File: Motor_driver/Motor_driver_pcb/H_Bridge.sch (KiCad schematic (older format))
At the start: 8 parts, among them Q1 IRF9540N, Q2 IRF540N, Q3 IRF9540N, Q4 IRF540N

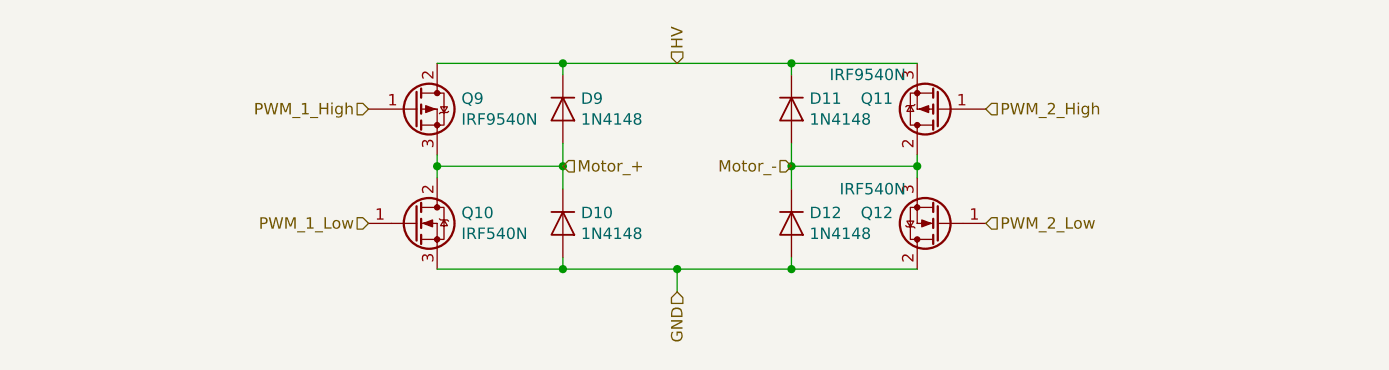
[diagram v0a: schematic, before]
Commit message: update driver schema add  uc config
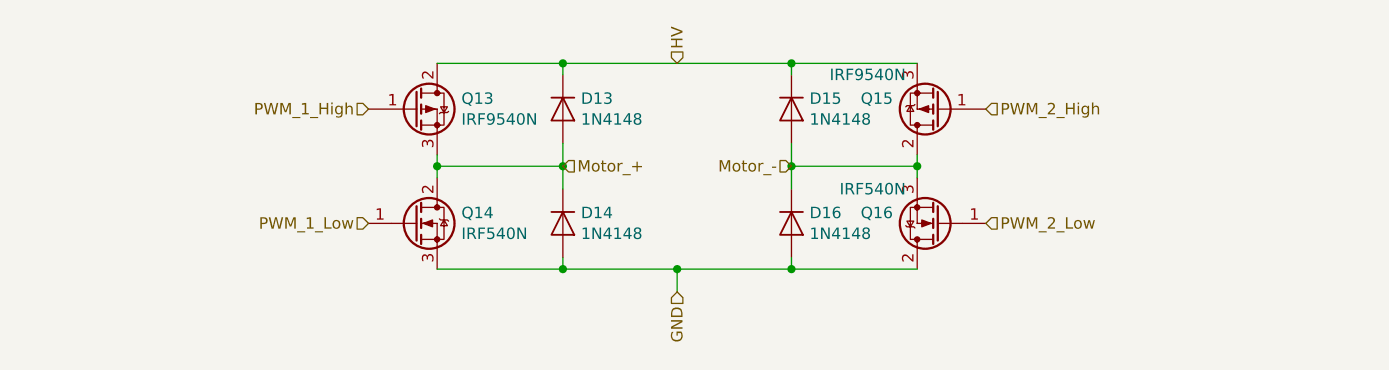
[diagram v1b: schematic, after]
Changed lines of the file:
@@
 $Descr A4 11693 8268
 encoding utf-8
-Sheet 4 5
+Sheet 5 5
 Title ""
 Date ""
@@
 AR Path="/5C9F4B73/5C9E42AA" Ref="Q10"  Part="1"
 AR Path="/5C9F4B7D/5C9E42AA" Ref="Q14"  Part="1"
-F 0 "Q10" H 4056 3046 50  0000 L CNN
+F 0 "Q14" H 4056 3046 50  0000 L CNN
 F 1 "IRF540N" H 4056 2955 50  0000 L CNN
 F 2 "Package_TO_SOT_THT:TO-220-3_Vertical" H 4100 2925 50  0001 L CIN
@@
 AR Path="/5C9F4B73/5C9E4811" Ref="Q9"  Part="1"
 AR Path="/5C9F4B7D/5C9E4811" Ref="Q13"  Part="1"
-F 0 "Q9" H 4056 2546 50  0000 L CNN
+F 0 "Q13" H 4056 2546 50  0000 L CNN
 F 1 "IRF9540N" H 4056 2455 50  0000 L CNN
 F 2 "Package_TO_SOT_THT:TO-220-3_Vertical" H 4050 2425 50  0001 L CIN
@@
 AR Path="/5C9F4B73/5C9E549E" Ref="D9"  Part="1"
 AR Path="/5C9F4B7D/5C9E549E" Ref="D13"  Part="1"
-F 0 "D9" V 4454 2579 50  0000 L CNN
+F 0 "D13" V 4454 2579 50  0000 L CNN
 F 1 "1N4148" V 4545 2579 50  0000 L CNN
 F 2 "Diode_THT:D_DO-35_SOD27_P7.62mm_Horizontal" H 4500 2325 50  0001 C CNN
@@
 AR Path="/5C9F4B73/5C9E5F82" Ref="D10"  Part="1"
 AR Path="/5C9F4B7D/5C9E5F82" Ref="D14"  Part="1"
-F 0 "D10" V 4454 3079 50  0000 L CNN
+F 0 "D14" V 4454 3079 50  0000 L CNN
 F 1 "1N4148" V 4545 3079 50  0000 L CNN
 F 2 "Diode_THT:D_DO-35_SOD27_P7.62mm_Horizontal" H 4500 2825 50  0001 C CNN
@@
 AR Path="/5C9F4B73/5C9E6D79" Ref="Q11"  Part="1"
 AR Path="/5C9F4B7D/5C9E6D79" Ref="Q15"  Part="1"
-F 0 "Q11" H 6356 2454 50  0000 L CNN
+F 0 "Q15" H 6356 2454 50  0000 L CNN
 F 1 "IRF9540N" H 6300 2350 50  0000 L CNN
 F 2 "Package_TO_SOT_THT:TO-220-3_Vertical" H 6350 2425 50  0001 L CIN
@@
 AR Path="/5C9F4B73/5C9E8C92" Ref="Q12"  Part="1"
 AR Path="/5C9F4B7D/5C9E8C92" Ref="Q16"  Part="1"
-F 0 "Q12" H 6356 2954 50  0000 L CNN
+F 0 "Q16" H 6356 2954 50  0000 L CNN
 F 1 "IRF540N" H 6300 2850 50  0000 L CNN
 F 2 "Package_TO_SOT_THT:TO-220-3_Vertical" H 6400 2925 50  0001 L CIN
@@
 AR Path="/5C9F4B73/5C9EAA23" Ref="D11"  Part="1"
 AR Path="/5C9F4B7D/5C9EAA23" Ref="D15"  Part="1"
-F 0 "D11" V 5454 2579 50  0000 L CNN
+F 0 "D15" V 5454 2579 50  0000 L CNN
 F 1 "1N4148" V 5545 2579 50  0000 L CNN
 F 2 "Diode_THT:D_DO-35_SOD27_P7.62mm_Horizontal" H 5500 2325 50  0001 C CNN
@@
 AR Path="/5C9F4B73/5C9EC3FB" Ref="D12"  Part="1"
 AR Path="/5C9F4B7D/5C9EC3FB" Ref="D16"  Part="1"
-F 0 "D12" V 5454 3079 50  0000 L CNN
+F 0 "D16" V 5454 3079 50  0000 L CNN
 F 1 "1N4148" V 5545 3079 50  0000 L CNN
 F 2 "Diode_THT:D_DO-35_SOD27_P7.62mm_Horizontal" H 5500 2825 50  0001 C CNN

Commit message: update schema, create PCB
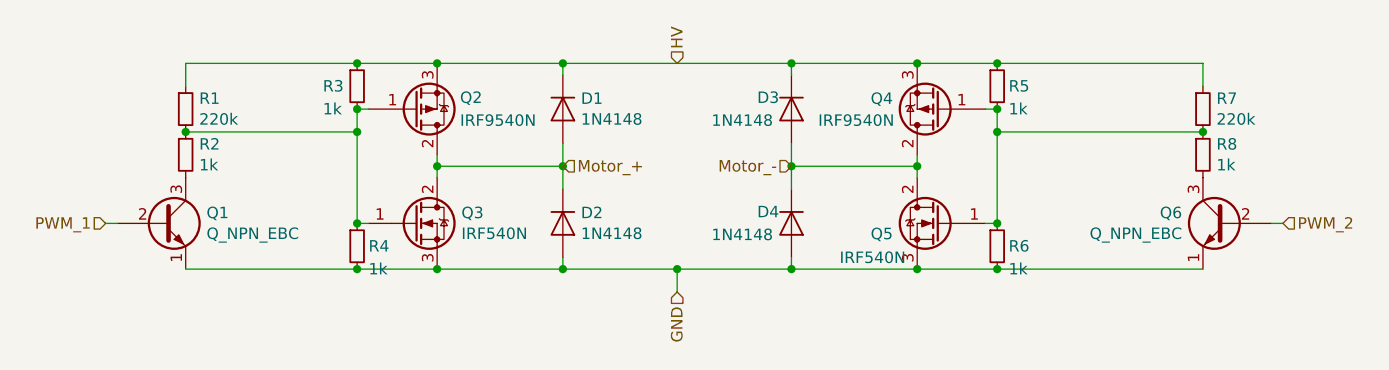
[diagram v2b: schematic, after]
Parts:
- added Q1, Q6: Q_NPN_EBC, Package_TO_SOT_THT:TO-92, symbol Device:Q_NPN_EBC
- added R1, R7: 220k, Resistor_SMD:R_0805_2012Metric_Pad1.15x1.40mm_HandSolder, symbol Device:R_Small
- added R2, R3, R4, R5, R6, R8: 1k, Resistor_SMD:R_0805_2012Metric_Pad1.15x1.40mm_HandSolder, symbol Device:R_Small
- renumbered Q1 to Q2, Q2 to Q3, Q3 to Q4, Q4 to Q5
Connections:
- net PWM_1_Low is gone; now on an unnamed net: Q3.1 (G)
- net PWM_2_Low is gone; now on an unnamed net: Q5.1 (G)
- net GND: now also Q5.3 (S), Q1.1 (E), Q6.1 (E), R4.2, R6.2; no longer Q5.2 (D)
- net HV: now also Q2.3 (S), R1.1, R3.1, R5.1, R7.1; no longer Q2.2 (D)
- net Motor_+: now also Q2.2 (D); no longer Q2.3 (S)
- net Motor_-: now also Q5.2 (D); no longer Q5.3 (S)
- net PWM_1_High: no longer names the net of Q2.1 (G)
- net PWM_1_High: now also R1.2, R2.1, R3.2, R4.1
- net PWM_2_High: no longer names the net of Q4.1 (G)
- net PWM_2_High: now also R5.2, R6.1, R7.2, R8.1
- new net: Q1.3 (C), R2.2
- new net: Q6.3 (C), R8.2
- new net PWM_1: Q1.2 (B)
- new net PWM_2: Q6.2 (B)

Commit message: finish schema and PCB update uC configuration
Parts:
- Q1, Q6: value Q_NPN_EBC -> 2N2222
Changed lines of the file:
@@
 AR Path="/5CA227B5/5CC73221" Ref="Q19"  Part="1"
 F 0 "Q1" H 2941 3046 50  0000 L CNN
-F 1 "Q_NPN_EBC" H 2941 2955 50  0000 L CNN
+F 1 "2N2222" H 2941 2955 50  0000 L CNN
 F 2 "Package_TO_SOT_THT:TO-92" H 2950 3100 50  0001 C CNN
 F 3 "~" H 2750 3000 50  0001 C CNN
@@
 AR Path="/5CA227B5/5CC746B3" Ref="Q24"  Part="1"
 F 0 "Q6" H 7591 3046 50  0000 L CNN
-F 1 "Q_NPN_EBC" H 7591 2955 50  0000 L CNN
+F 1 "2N2222" H 7591 2955 50  0000 L CNN
 F 2 "Package_TO_SOT_THT:TO-92" H 7600 3100 50  0001 C CNN
 F 3 "~" H 7400 3000 50  0001 C CNN

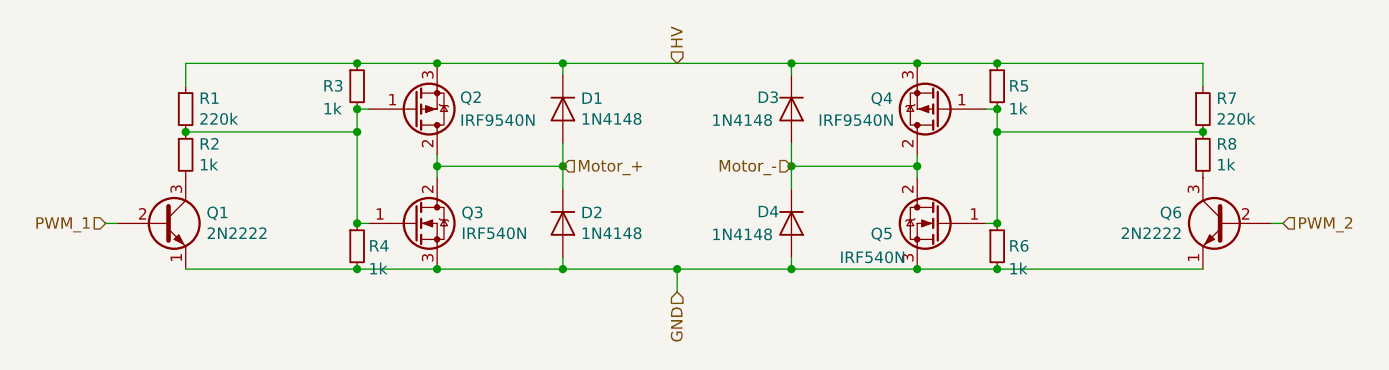
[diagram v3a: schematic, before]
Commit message: add BT_module PCB add Gerbera files
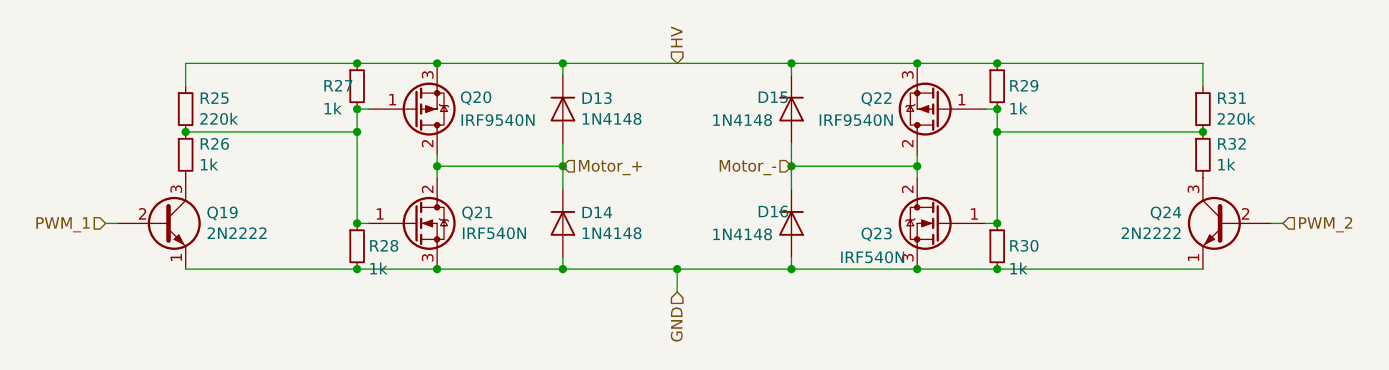
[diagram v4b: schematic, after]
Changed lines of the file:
@@
 AR Path="/5CA1B151/5C9E42AA" Ref="Q15"  Part="1"
 AR Path="/5CA227B5/5C9E42AA" Ref="Q21"  Part="1"
-F 0 "Q3" H 4056 3046 50  0000 L CNN
+F 0 "Q21" H 4056 3046 50  0000 L CNN
 F 1 "IRF540N" H 4056 2955 50  0000 L CNN
 F 2 "Package_TO_SOT_THT:TO-220-3_Vertical" H 4100 2925 50  0001 L CIN
@@
 AR Path="/5CA1B151/5C9E4811" Ref="Q14"  Part="1"
 AR Path="/5CA227B5/5C9E4811" Ref="Q20"  Part="1"
-F 0 "Q2" H 4050 2450 50  0000 L CNN
+F 0 "Q20" H 4050 2450 50  0000 L CNN
 F 1 "IRF9540N" H 4050 2550 50  0000 L CNN
 F 2 "Package_TO_SOT_THT:TO-220-3_Vertical" H 4050 2425 50  0001 L CIN
@@
 AR Path="/5CA1B151/5C9E549E" Ref="D9"  Part="1"
 AR Path="/5CA227B5/5C9E549E" Ref="D13"  Part="1"
-F 0 "D1" V 4454 2579 50  0000 L CNN
+F 0 "D13" V 4454 2579 50  0000 L CNN
 F 1 "1N4148" V 4545 2579 50  0000 L CNN
 F 2 "Diode_THT:D_DO-35_SOD27_P7.62mm_Horizontal" H 4500 2325 50  0001 C CNN
@@
 AR Path="/5CA1B151/5C9E5F82" Ref="D10"  Part="1"
 AR Path="/5CA227B5/5C9E5F82" Ref="D14"  Part="1"
-F 0 "D2" V 4454 3079 50  0000 L CNN
+F 0 "D14" V 4454 3079 50  0000 L CNN
 F 1 "1N4148" V 4545 3079 50  0000 L CNN
 F 2 "Diode_THT:D_DO-35_SOD27_P7.62mm_Horizontal" H 4500 2825 50  0001 C CNN
@@
 AR Path="/5CA1B151/5C9E6D79" Ref="Q16"  Part="1"
 AR Path="/5CA227B5/5C9E6D79" Ref="Q22"  Part="1"
-F 0 "Q4" H 6356 2454 50  0000 L CNN
+F 0 "Q22" H 6356 2454 50  0000 L CNN
 F 1 "IRF9540N" H 6350 2550 50  0000 L CNN
 F 2 "Package_TO_SOT_THT:TO-220-3_Vertical" H 6350 2425 50  0001 L CIN
@@
 AR Path="/5CA1B151/5C9E8C92" Ref="Q17"  Part="1"
 AR Path="/5CA227B5/5C9E8C92" Ref="Q23"  Part="1"
-F 0 "Q5" H 6356 2954 50  0000 L CNN
+F 0 "Q23" H 6356 2954 50  0000 L CNN
 F 1 "IRF540N" H 6300 2850 50  0000 L CNN
 F 2 "Package_TO_SOT_THT:TO-220-3_Vertical" H 6400 2925 50  0001 L CIN
@@
 AR Path="/5CA1B151/5C9EAA23" Ref="D11"  Part="1"
 AR Path="/5CA227B5/5C9EAA23" Ref="D15"  Part="1"
-F 0 "D3" V 5450 2350 50  0000 L CNN
+F 0 "D15" V 5450 2350 50  0000 L CNN
 F 1 "1N4148" V 5550 2150 50  0000 L CNN
 F 2 "Diode_THT:D_DO-35_SOD27_P7.62mm_Horizontal" H 5500 2325 50  0001 C CNN
@@
 AR Path="/5CA1B151/5C9EC3FB" Ref="D12"  Part="1"
 AR Path="/5CA227B5/5C9EC3FB" Ref="D16"  Part="1"
-F 0 "D4" V 5450 2850 50  0000 L CNN
+F 0 "D16" V 5450 2850 50  0000 L CNN
 F 1 "1N4148" V 5550 2650 50  0000 L CNN
 F 2 "Diode_THT:D_DO-35_SOD27_P7.62mm_Horizontal" H 5500 2825 50  0001 C CNN
@@
 AR Path="/5CA1B151/5CA04B0F" Ref="R21"  Part="1"
 AR Path="/5CA227B5/5CA04B0F" Ref="R29"  Part="1"
-F 0 "R5" H 6450 2400 50  0000 L CNN
+F 0 "R29" H 6450 2400 50  0000 L CNN
 F 1 "1k" H 6450 2300 50  0000 L CNN
 F 2 "Resistor_SMD:R_0805_2012Metric_Pad1.15x1.40mm_HandSolder" H 6400 2400 50  0001 C CNN
@@
 AR Path="/5CA1B151/5CA04F40" Ref="R22"  Part="1"
 AR Path="/5CA227B5/5CA04F40" Ref="R30"  Part="1"
-F 0 "R6" H 6450 3100 50  0000 L CNN
+F 0 "R30" H 6450 3100 50  0000 L CNN
 F 1 "1k" H 6450 3000 50  0000 L CNN
 F 2 "Resistor_SMD:R_0805_2012Metric_Pad1.15x1.40mm_HandSolder" H 6400 3100 50  0001 C CNN
@@
 AR Path="/5CA1B151/5CA0523E" Ref="R20"  Part="1"
 AR Path="/5CA227B5/5CA0523E" Ref="R28"  Part="1"
-F 0 "R4" H 3650 3100 50  0000 L CNN
+F 0 "R28" H 3650 3100 50  0000 L CNN
 F 1 "1k" H 3650 3000 50  0000 L CNN
 F 2 "Resistor_SMD:R_0805_2012Metric_Pad1.15x1.40mm_HandSolder" H 3600 3100 50  0001 C CNN
@@
 AR Path="/5CA1B151/5CA057A9" Ref="R19"  Part="1"
 AR Path="/5CA227B5/5CA057A9" Ref="R27"  Part="1"
-F 0 "R3" H 3450 2400 50  0000 L CNN
+F 0 "R27" H 3450 2400 50  0000 L CNN
 F 1 "1k" H 3450 2300 50  0000 L CNN
 F 2 "Resistor_SMD:R_0805_2012Metric_Pad1.15x1.40mm_HandSolder" H 3600 2400 50  0001 C CNN
@@
 AR Path="/5CA1B151/5CABFFC4" Ref="R18"  Part="1"
 AR Path="/5CA227B5/5CABFFC4" Ref="R26"  Part="1"
-F 0 "R2" H 2909 2746 50  0000 L CNN
+F 0 "R26" H 2909 2746 50  0000 L CNN
 F 1 "1k" H 2909 2655 50  0000 L CNN
 F 2 "Resistor_SMD:R_0805_2012Metric_Pad1.15x1.40mm_HandSolder" H 2850 2700 50  0001 C CNN
@@
 AR Path="/5CA1B151/5CAC04F6" Ref="R17"  Part="1"
 AR Path="/5CA227B5/5CAC04F6" Ref="R25"  Part="1"
-F 0 "R1" H 2909 2546 50  0000 L CNN
+F 0 "R25" H 2909 2546 50  0000 L CNN
 F 1 "220k" H 2909 2455 50  0000 L CNN
 F 2 "Resistor_SMD:R_0805_2012Metric_Pad1.15x1.40mm_HandSolder" H 2850 2500 50  0001 C CNN
@@
 AR Path="/5CA1B151/5CBAE7DE" Ref="R24"  Part="1"
 AR Path="/5CA227B5/5CBAE7DE" Ref="R32"  Part="1"
-F 0 "R8" H 7359 2746 50  0000 L CNN
+F 0 "R32" H 7359 2746 50  0000 L CNN
 F 1 "1k" H 7359 2655 50  0000 L CNN
 F 2 "Resistor_SMD:R_0805_2012Metric_Pad1.15x1.40mm_HandSolder" H 7300 2700 50  0001 C CNN
@@
 AR Path="/5CA1B151/5CBAE7E4" Ref="R23"  Part="1"
 AR Path="/5CA227B5/5CBAE7E4" Ref="R31"  Part="1"
-F 0 "R7" H 7359 2546 50  0000 L CNN
+F 0 "R31" H 7359 2546 50  0000 L CNN
 F 1 "220k" H 7359 2455 50  0000 L CNN
 F 2 "Resistor_SMD:R_0805_2012Metric_Pad1.15x1.40mm_HandSolder" H 7300 2500 50  0001 C CNN
@@
 AR Path="/5CA1B151/5CC73221" Ref="Q13"  Part="1"
 AR Path="/5CA227B5/5CC73221" Ref="Q19"  Part="1"
-F 0 "Q1" H 2941 3046 50  0000 L CNN
+F 0 "Q19" H 2941 3046 50  0000 L CNN
 F 1 "2N2222" H 2941 2955 50  0000 L CNN
 F 2 "Package_TO_SOT_THT:TO-92" H 2950 3100 50  0001 C CNN
@@
 AR Path="/5CA1B151/5CC746B3" Ref="Q18"  Part="1"
 AR Path="/5CA227B5/5CC746B3" Ref="Q24"  Part="1"
-F 0 "Q6" H 7591 3046 50  0000 L CNN
+F 0 "Q24" H 7591 3046 50  0000 L CNN
 F 1 "2N2222" H 7591 2955 50  0000 L CNN
 F 2 "Package_TO_SOT_THT:TO-92" H 7600 3100 50  0001 C CNN

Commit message: add final parts and working code
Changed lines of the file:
@@
 AR Path="/5CA1B151/5C9E42AA" Ref="Q15"  Part="1"
 AR Path="/5CA227B5/5C9E42AA" Ref="Q21"  Part="1"
-F 0 "Q21" H 4056 3046 50  0000 L CNN
+F 0 "Q3" H 4056 3046 50  0000 L CNN
 F 1 "IRF540N" H 4056 2955 50  0000 L CNN
 F 2 "Package_TO_SOT_THT:TO-220-3_Vertical" H 4100 2925 50  0001 L CIN
@@
 AR Path="/5CA1B151/5C9E4811" Ref="Q14"  Part="1"
 AR Path="/5CA227B5/5C9E4811" Ref="Q20"  Part="1"
-F 0 "Q20" H 4050 2450 50  0000 L CNN
+F 0 "Q2" H 4050 2450 50  0000 L CNN
 F 1 "IRF9540N" H 4050 2550 50  0000 L CNN
 F 2 "Package_TO_SOT_THT:TO-220-3_Vertical" H 4050 2425 50  0001 L CIN
@@
 AR Path="/5CA1B151/5C9E549E" Ref="D9"  Part="1"
 AR Path="/5CA227B5/5C9E549E" Ref="D13"  Part="1"
-F 0 "D13" V 4454 2579 50  0000 L CNN
+F 0 "D1" V 4454 2579 50  0000 L CNN
 F 1 "1N4148" V 4545 2579 50  0000 L CNN
 F 2 "Diode_THT:D_DO-35_SOD27_P7.62mm_Horizontal" H 4500 2325 50  0001 C CNN
@@
 AR Path="/5CA1B151/5C9E5F82" Ref="D10"  Part="1"
 AR Path="/5CA227B5/5C9E5F82" Ref="D14"  Part="1"
-F 0 "D14" V 4454 3079 50  0000 L CNN
+F 0 "D2" V 4454 3079 50  0000 L CNN
 F 1 "1N4148" V 4545 3079 50  0000 L CNN
 F 2 "Diode_THT:D_DO-35_SOD27_P7.62mm_Horizontal" H 4500 2825 50  0001 C CNN
@@
 AR Path="/5CA1B151/5C9E6D79" Ref="Q16"  Part="1"
 AR Path="/5CA227B5/5C9E6D79" Ref="Q22"  Part="1"
-F 0 "Q22" H 6356 2454 50  0000 L CNN
+F 0 "Q4" H 6356 2454 50  0000 L CNN
 F 1 "IRF9540N" H 6350 2550 50  0000 L CNN
 F 2 "Package_TO_SOT_THT:TO-220-3_Vertical" H 6350 2425 50  0001 L CIN
@@
 AR Path="/5CA1B151/5C9E8C92" Ref="Q17"  Part="1"
 AR Path="/5CA227B5/5C9E8C92" Ref="Q23"  Part="1"
-F 0 "Q23" H 6356 2954 50  0000 L CNN
+F 0 "Q5" H 6356 2954 50  0000 L CNN
 F 1 "IRF540N" H 6300 2850 50  0000 L CNN
 F 2 "Package_TO_SOT_THT:TO-220-3_Vertical" H 6400 2925 50  0001 L CIN
@@
 AR Path="/5CA1B151/5C9EAA23" Ref="D11"  Part="1"
 AR Path="/5CA227B5/5C9EAA23" Ref="D15"  Part="1"
-F 0 "D15" V 5450 2350 50  0000 L CNN
+F 0 "D3" V 5450 2350 50  0000 L CNN
 F 1 "1N4148" V 5550 2150 50  0000 L CNN
 F 2 "Diode_THT:D_DO-35_SOD27_P7.62mm_Horizontal" H 5500 2325 50  0001 C CNN
@@
 AR Path="/5CA1B151/5C9EC3FB" Ref="D12"  Part="1"
 AR Path="/5CA227B5/5C9EC3FB" Ref="D16"  Part="1"
-F 0 "D16" V 5450 2850 50  0000 L CNN
+F 0 "D4" V 5450 2850 50  0000 L CNN
 F 1 "1N4148" V 5550 2650 50  0000 L CNN
 F 2 "Diode_THT:D_DO-35_SOD27_P7.62mm_Horizontal" H 5500 2825 50  0001 C CNN
@@
 Wire Wire Line
 	4500 3200 5000 3200
-Text HLabel 2500 3000 0    50   Input ~ 0
+Text HLabel 2500 3000 0    50   Input ~ 10
 PWM_1
-Text HLabel 7650 3000 2    50   Input ~ 0
+Text HLabel 7650 3000 2    50   Input ~ 10
 PWM_2
-Text HLabel 5000 3300 3    50   Input ~ 0
+Text HLabel 5000 3300 3    50   Input ~ 10
 GND
 Wire Wire Line
@@
 Connection ~ 4500 2300
 Connection ~ 5500 2300
-Text HLabel 5000 2300 1    50   Input ~ 0
+Text HLabel 5000 2300 1    50   Input ~ 10
 HV
-Text HLabel 4500 2750 2    50   Input ~ 0
+Text HLabel 4500 2750 2    50   Input ~ 10
 Motor_+
-Text HLabel 5500 2750 0    50   Input ~ 0
+Text HLabel 5500 2750 0    50   Input ~ 10
 Motor_-
 $Comp
@@
 AR Path="/5CA1B151/5CA04B0F" Ref="R21"  Part="1"
 AR Path="/5CA227B5/5CA04B0F" Ref="R29"  Part="1"
-F 0 "R29" H 6450 2400 50  0000 L CNN
+F 0 "R5" H 6450 2400 50  0000 L CNN
 F 1 "1k" H 6450 2300 50  0000 L CNN
 F 2 "Resistor_SMD:R_0805_2012Metric_Pad1.15x1.40mm_HandSolder" H 6400 2400 50  0001 C CNN
@@
 AR Path="/5CA1B151/5CA04F40" Ref="R22"  Part="1"
 AR Path="/5CA227B5/5CA04F40" Ref="R30"  Part="1"
-F 0 "R30" H 6450 3100 50  0000 L CNN
+F 0 "R6" H 6450 3100 50  0000 L CNN
 F 1 "1k" H 6450 3000 50  0000 L CNN
 F 2 "Resistor_SMD:R_0805_2012Metric_Pad1.15x1.40mm_HandSolder" H 6400 3100 50  0001 C CNN
@@
 AR Path="/5CA1B151/5CA0523E" Ref="R20"  Part="1"
 AR Path="/5CA227B5/5CA0523E" Ref="R28"  Part="1"
-F 0 "R28" H 3650 3100 50  0000 L CNN
+F 0 "R4" H 3650 3100 50  0000 L CNN
 F 1 "1k" H 3650 3000 50  0000 L CNN
 F 2 "Resistor_SMD:R_0805_2012Metric_Pad1.15x1.40mm_HandSolder" H 3600 3100 50  0001 C CNN
@@
 AR Path="/5CA1B151/5CA057A9" Ref="R19"  Part="1"
 AR Path="/5CA227B5/5CA057A9" Ref="R27"  Part="1"
-F 0 "R27" H 3450 2400 50  0000 L CNN
+F 0 "R3" H 3450 2400 50  0000 L CNN
 F 1 "1k" H 3450 2300 50  0000 L CNN
 F 2 "Resistor_SMD:R_0805_2012Metric_Pad1.15x1.40mm_HandSolder" H 3600 2400 50  0001 C CNN
@@
 AR Path="/5CA1B151/5CABFFC4" Ref="R18"  Part="1"
 AR Path="/5CA227B5/5CABFFC4" Ref="R26"  Part="1"
-F 0 "R26" H 2909 2746 50  0000 L CNN
+F 0 "R2" H 2909 2746 50  0000 L CNN
 F 1 "1k" H 2909 2655 50  0000 L CNN
 F 2 "Resistor_SMD:R_0805_2012Metric_Pad1.15x1.40mm_HandSolder" H 2850 2700 50  0001 C CNN
@@
 AR Path="/5CA1B151/5CAC04F6" Ref="R17"  Part="1"
 AR Path="/5CA227B5/5CAC04F6" Ref="R25"  Part="1"
-F 0 "R25" H 2909 2546 50  0000 L CNN
+F 0 "R1" H 2909 2546 50  0000 L CNN
 F 1 "220k" H 2909 2455 50  0000 L CNN
 F 2 "Resistor_SMD:R_0805_2012Metric_Pad1.15x1.40mm_HandSolder" H 2850 2500 50  0001 C CNN
@@
 AR Path="/5CA1B151/5CBAE7DE" Ref="R24"  Part="1"
 AR Path="/5CA227B5/5CBAE7DE" Ref="R32"  Part="1"
-F 0 "R32" H 7359 2746 50  0000 L CNN
+F 0 "R8" H 7359 2746 50  0000 L CNN
 F 1 "1k" H 7359 2655 50  0000 L CNN
 F 2 "Resistor_SMD:R_0805_2012Metric_Pad1.15x1.40mm_HandSolder" H 7300 2700 50  0001 C CNN
@@
 AR Path="/5CA1B151/5CBAE7E4" Ref="R23"  Part="1"
 AR Path="/5CA227B5/5CBAE7E4" Ref="R31"  Part="1"
-F 0 "R31" H 7359 2546 50  0000 L CNN
+F 0 "R7" H 7359 2546 50  0000 L CNN
 F 1 "220k" H 7359 2455 50  0000 L CNN
 F 2 "Resistor_SMD:R_0805_2012Metric_Pad1.15x1.40mm_HandSolder" H 7300 2500 50  0001 C CNN
@@
 AR Path="/5CA1B151/5CC73221" Ref="Q13"  Part="1"
 AR Path="/5CA227B5/5CC73221" Ref="Q19"  Part="1"
-F 0 "Q19" H 2941 3046 50  0000 L CNN
+F 0 "Q1" H 2941 3046 50  0000 L CNN
 F 1 "2N2222" H 2941 2955 50  0000 L CNN
 F 2 "Package_TO_SOT_THT:TO-92" H 2950 3100 50  0001 C CNN
@@
 AR Path="/5CA1B151/5CC746B3" Ref="Q18"  Part="1"
 AR Path="/5CA227B5/5CC746B3" Ref="Q24"  Part="1"
-F 0 "Q24" H 7591 3046 50  0000 L CNN
+F 0 "Q6" H 7591 3046 50  0000 L CNN
 F 1 "2N2222" H 7591 2955 50  0000 L CNN
 F 2 "Package_TO_SOT_THT:TO-92" H 7600 3100 50  0001 C CNN
